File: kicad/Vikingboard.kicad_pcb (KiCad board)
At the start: 2 copper layers, 9 parts, among them J1 Conn_02x09_Odd_Even, J2 Conn_02x18_Odd_Even, U1 Conn_01x05, U2 DRV2605LDGS, U3 PAL24, U4 Q_Triac, U5 SX1276, U6 Conn_02x04_Odd_Even_Shielded, U7 Conn_01x08_Shielded

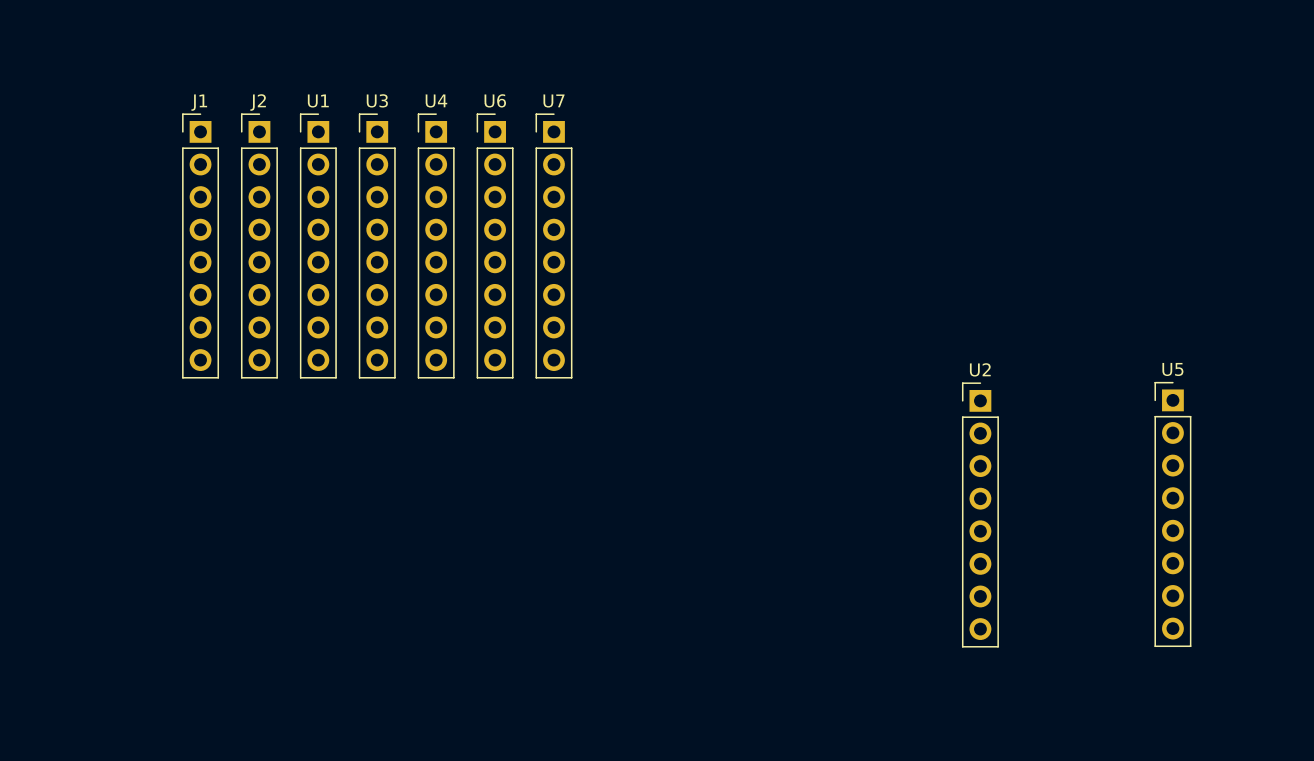
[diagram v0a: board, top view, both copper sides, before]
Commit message: PCB Update - 2025-12-05 12:30
✅ Production files updated
- Gerbers regenerated
- DRC passed
- Ready for manufacturing

Changes:
  - kicad/vikingboard_gerbers.zip
  - pcb_scripts/vikingboard_bom_jlcpcb.csv
  - pcb_scripts/vikingboard_cpl.csv
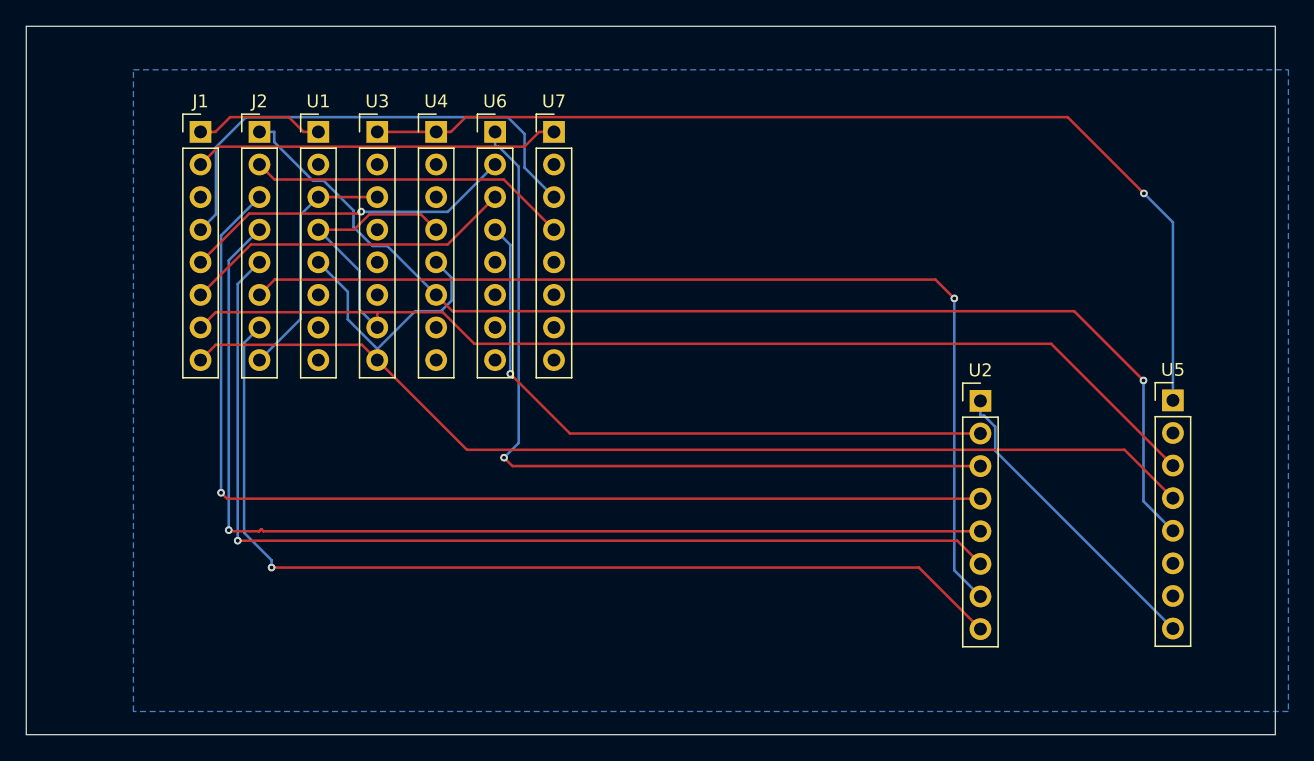
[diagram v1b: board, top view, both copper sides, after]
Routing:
- net SPI_SCK: track 0.00 -> 102.1 mm
- net SPI_MOSI: track 0.00 -> 101.6 mm
- net SPI_MISO: track 0.00 -> 90.8 mm, vias 0 -> 1
- net FZ_GPIO1: track 0.00 -> 83.6 mm, vias 0 -> 1
- net FZ_GPIO2: track 0.00 -> 83.4 mm, vias 0 -> 1
- net FZ_GPIO3: track 0.00 -> 81.0 mm, vias 0 -> 1
- net +3V3_RF: track 0.00 -> 79.7 mm, vias 0 -> 1
- net FZ_GPIO4: track 0.00 -> 79.3 mm, vias 0 -> 1
- net FZ_GPIO5: track 0.00 -> 77.3 mm, vias 0 -> 1
- net KBD_INT: track 0.00 -> 64.2 mm, vias 0 -> 1
- net KBD_RST: track 0.00 -> 50.3 mm, vias 0 -> 1
- net GPS_RX: track 0.00 -> 38.4 mm
- net +3V3_IO: track 0.00 -> 28.6 mm
- net I2C_SCL: track 0.00 -> 26.1 mm, vias 0 -> 1
- net I2C_SDA: track 0.00 -> 26.1 mm
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- added copper zone on B.Cu, net GND
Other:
- board outline added: 97.3 x 55.2 mm
